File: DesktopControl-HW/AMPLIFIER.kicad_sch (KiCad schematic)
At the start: 20 parts, among them IC401 OPA172IDBVT, IC402 OPA172IDBVT, IC403 OPA172IDBVT, IC404 TLV1701AIDCKT

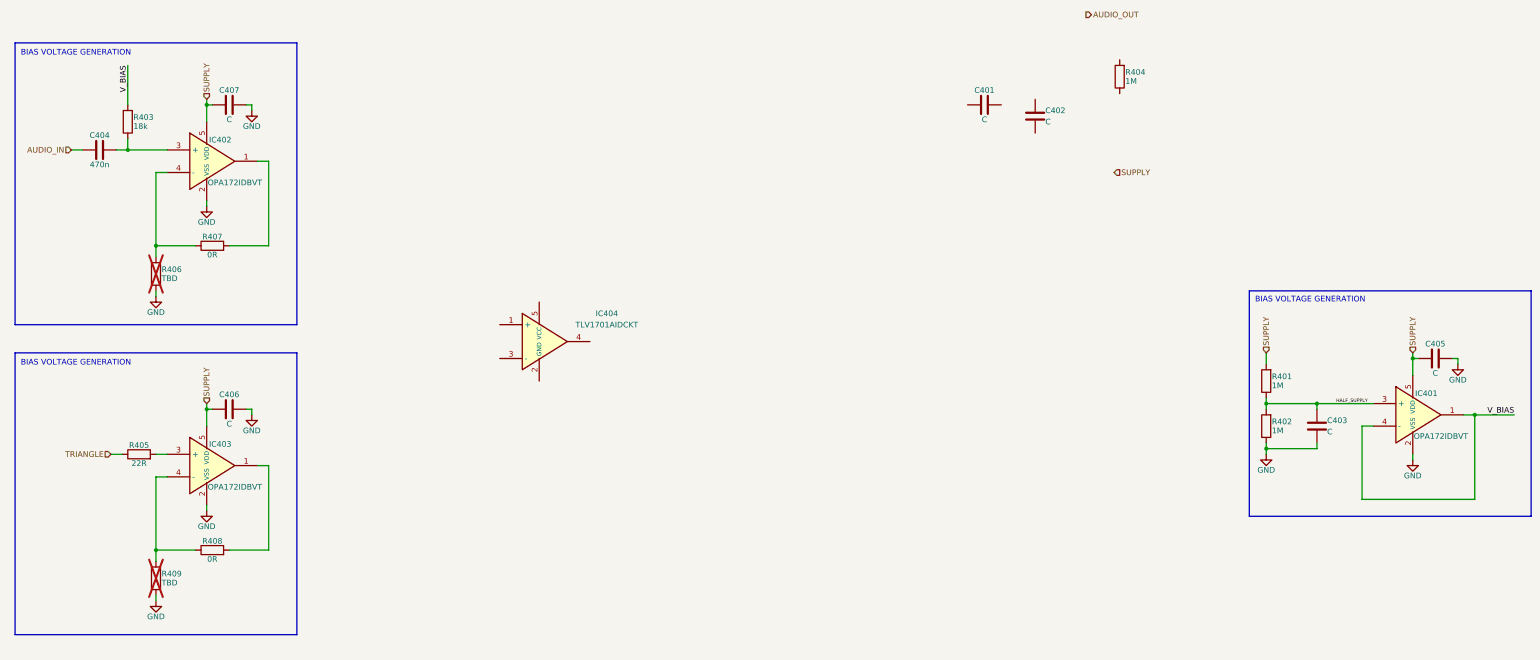
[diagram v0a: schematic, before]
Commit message: Rework amplifier configuration, add amplifier for subwoofer and start check of codec
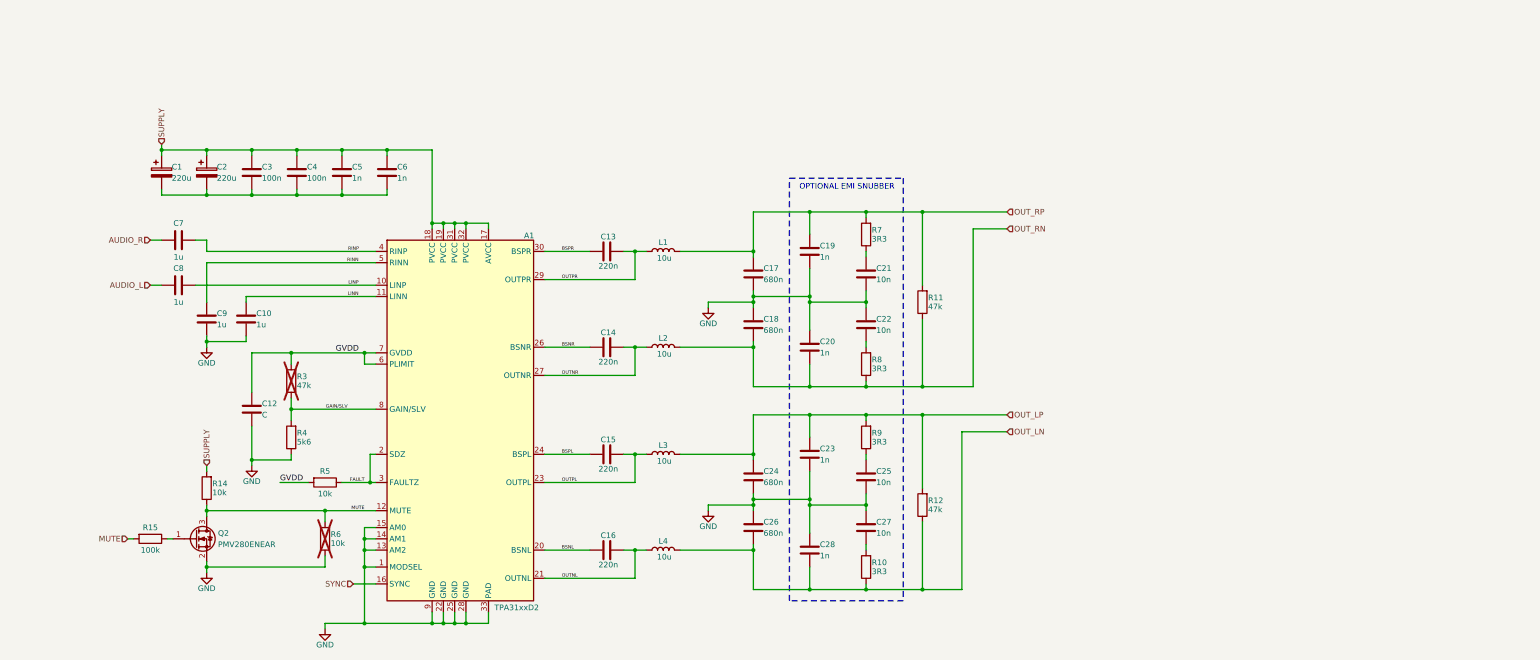
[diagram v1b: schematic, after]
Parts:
- removed C401, C402, C403, C405, C406, C407: C, Capacitor_SMD:C_0603_1608Metric_Pad1.08x0.95mm_HandSolder, symbol Device:C
- removed C404: 470n, Capacitor_SMD:C_0603_1608Metric_Pad1.08x0.95mm_HandSolder, symbol Device:C
- removed IC401, IC402, IC403: OPA172IDBVT, Lund Formula Student:SOT95P280X145-5N, symbol Lund Formula Student:OPA172IDBVT
- removed IC404: TLV1701AIDCKT, Lund Formula Student:SOT65P210X110-5N, symbol Lund Formula Student:TLV1701AIDCKT
- removed R401, R402, R404: 1M, Resistor_SMD:R_0603_1608Metric_Pad0.98x0.95mm_HandSolder, symbol Device:R
- removed R403: 18k, Resistor_SMD:R_0603_1608Metric_Pad0.98x0.95mm_HandSolder, symbol Device:R
- removed R405: 22R, Resistor_SMD:R_0603_1608Metric_Pad0.98x0.95mm_HandSolder, symbol Device:R
- removed R406, R409: TBD, Resistor_SMD:R_0603_1608Metric_Pad0.98x0.95mm_HandSolder, symbol Device:R
- removed R407, R408: 0R, Resistor_SMD:R_0603_1608Metric_Pad0.98x0.95mm_HandSolder, symbol Device:R
- added A1: TPA31xxD2, symbol AlfredLib:TPA31xxD2
- added C1, C2: 220u, symbol Device:C_Polarized
- added C10, C7, C8, C9: 1u, Capacitor_SMD:C_0603_1608Metric_Pad1.08x0.95mm_HandSolder, symbol Device:C
- added C12: C, Capacitor_SMD:C_0603_1608Metric_Pad1.08x0.95mm_HandSolder, symbol Device:C
- added C13, C14, C15, C16: 220n, Capacitor_SMD:C_0603_1608Metric_Pad1.08x0.95mm_HandSolder, symbol Device:C
- added C17, C18, C24, C26: 680n, Capacitor_SMD:C_0603_1608Metric_Pad1.08x0.95mm_HandSolder, symbol Device:C
- added C19, C20, C23, C28, C5, C6: 1n, Capacitor_SMD:C_0603_1608Metric_Pad1.08x0.95mm_HandSolder, symbol Device:C
- added C21, C22, C25, C27: 10n, Capacitor_SMD:C_0603_1608Metric_Pad1.08x0.95mm_HandSolder, symbol Device:C
- added C3, C4: 100n, Capacitor_SMD:C_0603_1608Metric_Pad1.08x0.95mm_HandSolder, symbol Device:C
- added L1, L2, L3, L4: 10u, symbol Device:L
- added Q2: PMV280ENEAR, Lund Formula Student:SOT95P230X110-3N, symbol Lund Formula Student:PMV280ENEAR
- added R10, R7, R8, R9: 3R3, Resistor_SMD:R_0603_1608Metric_Pad0.98x0.95mm_HandSolder, symbol Device:R
- added R11, R12, R3: 47k, Resistor_SMD:R_0603_1608Metric_Pad0.98x0.95mm_HandSolder, symbol Device:R
- added R14, R5, R6: 10k, Resistor_SMD:R_0603_1608Metric_Pad0.98x0.95mm_HandSolder, symbol Device:R
- added R15: 100k, Resistor_SMD:R_0603_1608Metric_Pad0.98x0.95mm_HandSolder, symbol Device:R
- added R4: 5k6, Resistor_SMD:R_0603_1608Metric_Pad0.98x0.95mm_HandSolder, symbol Device:R
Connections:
- net GND: now also A1.1 (MODSEL), A1.13 (AM2), A1.14 (AM1), A1.15 (AM0), A1.22 (GND), A1.25 (GND), A1.28 (GND), A1.33 (PAD), A1.9 (GND), C10.2, C12.2, C17.2, C18.1, C19.2, C20.1, C21.2, C22.1, C23.2, C24.2, C25.2, C26.1, C27.1, C28.1, C9.2, Q2.2 (S), R4.1, R6.1
- net SUPPLY: now also A1.17 (AVCC), A1.18 (PVCC), A1.19 (PVCC), A1.31 (PVCC), A1.32 (PVCC), C1.1, C2.1, C3.1, C4.1, C5.1, C6.1, R14.2
- new net: C25.1, R9.1
- new net: C21.1, R7.1
- new net: C1.2, C2.2, C3.2, C4.2, C5.2, C6.2
- new net: C22.2, R8.2
- new net: Q2.1 (G), R15.1
- new net: C27.2, R10.2
- new net AUDIO_L: C8.1
- new net AUDIO_R: C7.1
- new net BSNL: A1.20 (BSNL), C16.1
- new net BSNR: A1.26 (BSNR), C14.1
- new net BSPL: A1.24 (BSPL), C15.1
- new net BSPR: A1.30 (BSPR), C13.1
- new net FAULT: A1.2 (SDZ), A1.3 (FAULTZ), R5.1
- new net GAIN/SLV: A1.8 (GAIN/SLV), R3.1, R4.2
- new net GVDD: A1.6 (PLIMIT), A1.7 (GVDD), C12.1, R3.2, R5.2
- new net LINN: A1.11 (LINN), C10.1
- new net LINP: A1.10 (LINP), C8.2
- new net MUTE: A1.12 (MUTE), Q2.3 (D), R14.1, R15.2, R6.2
- new net OUTNL: A1.21 (OUTNL), C16.2, L4.1
- new net OUTNR: A1.27 (OUTNR), C14.2, L2.1
- new net OUTPL: A1.23 (OUTPL), C15.2, L3.1
- new net OUTPR: A1.29 (OUTPR), C13.2, L1.1
- new net OUT_LN: C26.2, C28.2, L4.2, R10.1, R12.1
- new net OUT_LP: C23.1, C24.1, L3.2, R12.2, R9.2
- new net OUT_RN: C18.2, C20.2, L2.2, R11.1, R8.1
- new net OUT_RP: C17.1, C19.1, L1.2, R11.2, R7.2
- new net RINN: A1.5 (RINN), C9.1
- new net RINP: A1.4 (RINP), C7.2
- new net SYNC: A1.16 (SYNC)
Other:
- note added: "OPTIONAL EMI SNUBBER"
- note removed: "BIAS VOLTAGE GENERATION"
